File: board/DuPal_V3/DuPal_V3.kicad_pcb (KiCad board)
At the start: 2 copper layers, 124 parts, among them J1 ZIF Socket, J2 Debug Header, K1 G6K-2, Q1 2N3904, SW1 RESET, U1 Pico, U10 74HCT166, U11 74HCT166, U12 74HCT166, U13 SN74LV1T125DBV, U2 74HCT595, U3 74HCT595, U4 74HCT595, U5 74HCT595, U6 74HCT595, U7 74HCT02, U8 74HCT166, U9 74HCT166

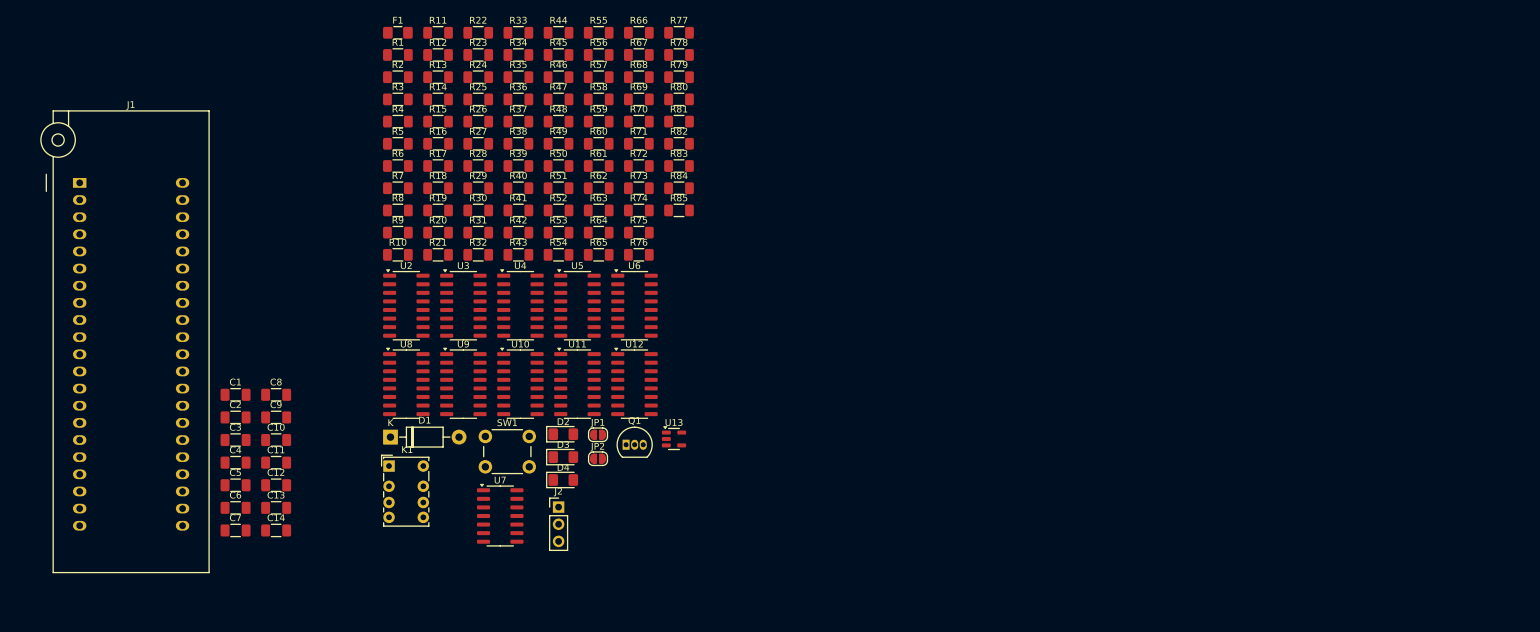
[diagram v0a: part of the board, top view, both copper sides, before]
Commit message: Begin organizing the footprint
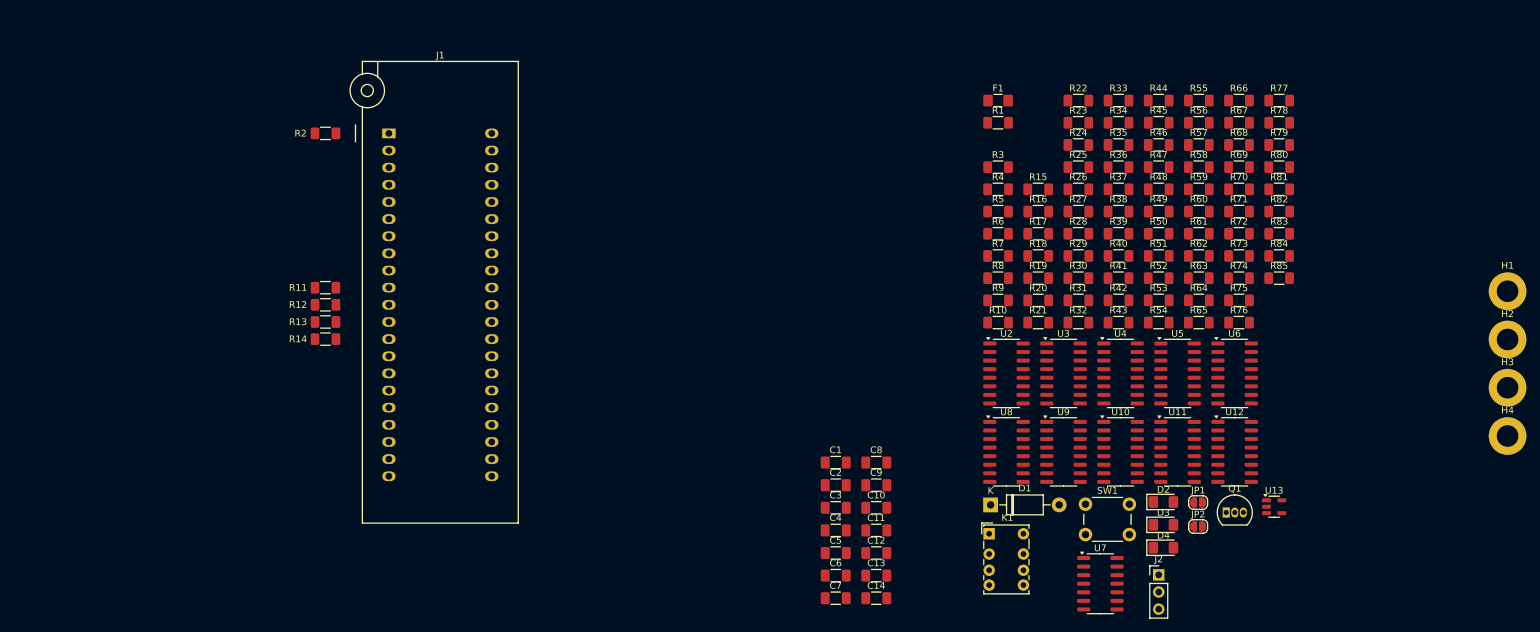
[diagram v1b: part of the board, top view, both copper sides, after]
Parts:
- added H1: MountingHole_Pad, MountingHole:MountingHole_3.2mm_M3_DIN965_Pad, F.Cu at (291.6, 79.8)
- added H2: MountingHole_Pad, MountingHole:MountingHole_3.2mm_M3_DIN965_Pad, F.Cu at (291.6, 86.9)
- added H3: MountingHole_Pad, MountingHole:MountingHole_3.2mm_M3_DIN965_Pad, F.Cu at (291.6, 94.1)
- added H4: MountingHole_Pad, MountingHole:MountingHole_3.2mm_M3_DIN965_Pad, F.Cu at (291.6, 101.2)
- R43: value 1K -> 1.2K
- moved F1 89.5 mm to (216.1, 51.5)
- moved R1 89.5 mm to (216.1, 54.8)
- moved R10 89.5 mm to (216.1, 84.4)
- moved R3 89.5 mm to (216.1, 61.4)
- moved R4 89.5 mm to (216.1, 64.7)
- moved R5 89.5 mm to (216.1, 68.0)
- moved R6 89.5 mm to (216.1, 71.3)
- moved R7 89.5 mm to (216.1, 74.5)
- moved R8 89.5 mm to (216.1, 77.8)
- moved R9 89.5 mm to (216.1, 81.1)
- moved C1 89.5 mm to (192.1, 105.2)
- moved C2 89.5 mm to (192.1, 108.5)
- moved C3 89.5 mm to (192.1, 111.9)
- moved C4 89.5 mm to (192.1, 115.2)
- moved C5 89.5 mm to (192.1, 118.6)
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
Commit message: Some more placing on the PCB
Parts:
- moved R15 108.5 mm to (116.5, 89.4)
- moved R16 108.3 mm to (116.5, 91.9)
- moved R17 108.1 mm to (116.5, 94.5)
- moved R18 108.0 mm to (116.5, 97.0)
- moved R19 107.8 mm to (116.5, 99.6)
- moved R20 107.7 mm to (116.5, 102.1)
- moved R21 107.5 mm to (116.5, 104.6)
- moved R10 99.9 mm to (116.5, 76.7)
- moved R9 99.9 mm to (116.5, 74.2)
- moved R8 99.8 mm to (116.5, 71.6)
- moved R7 99.8 mm to (116.5, 69.1)
- moved R6 99.8 mm to (116.5, 66.5)
- moved R5 99.7 mm to (116.5, 64.0)
- moved R4 99.7 mm to (116.5, 61.5)
- moved R3 99.7 mm to (116.5, 58.9)
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
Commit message: More board placing
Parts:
- R42, R46: moved to B.Cu
- moved R46 123.5 mm to (116.5, 56.4), turned to 180 degrees
- moved R33 88.1 mm to (150.3, 79.2), turned to 180 degrees
- moved R42 87.2 mm to (150.4, 56.4), turned to 180 degrees
- moved R34 86.4 mm to (150.3, 76.7), turned to 180 degrees
- moved R41 85.7 mm to (150.4, 58.9), turned to 180 degrees
- moved R35 85.1 mm to (150.4, 74.2), turned to 180 degrees
- moved R40 84.6 mm to (150.4, 61.5), turned to 180 degrees
- moved R36 84.2 mm to (150.4, 71.6), turned to 180 degrees
- moved R39 83.9 mm to (150.4, 64.0), turned to 180 degrees
- moved R37 83.7 mm to (150.4, 69.1), turned to 180 degrees
- moved R38 83.6 mm to (150.4, 66.5), turned to 180 degrees
- moved R27 82.0 mm to (150.4, 94.5), turned to 180 degrees
- moved R28 80.4 mm to (150.4, 91.9), turned to 180 degrees
- moved R29 79.1 mm to (150.4, 89.4), turned to 180 degrees
- moved R30 78.2 mm to (150.4, 86.9), turned to 180 degrees
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
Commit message: More placing
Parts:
- R47, R48, R49, R50, R51: moved to B.Cu
- moved R51 123.6 mm to (116.5, 69.1), turned to 180 degrees
- moved R50 123.5 mm to (116.5, 66.5), turned to 180 degrees
- moved R49 123.5 mm to (116.5, 64.0), turned to 180 degrees
- moved R48 123.5 mm to (116.5, 61.5), turned to 180 degrees
- moved R47 123.5 mm to (116.5, 58.9), turned to 180 degrees

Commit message: Update board
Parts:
- R46, R47, R48, R49, R50, R51, R53, R54, R55, R56, R57, R58, R59, R60, R61, R62, R63, R64, R65, R66, R67, R68, R69, R70, R71, R72, R73, R74, R75, R76, R77, R78, R79, R80, R81, R82, R83, R84, R85: value 100K -> 470K
- R52: value 100K -> 470K; moved to B.Cu
- moved R52 123.6 mm to (116.5, 71.6), turned to 180 degrees

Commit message: More placements
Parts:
- R53, R54, R55, R56, R57, R58, R59, R60, R61, R62, R63, R64, R65, R66, U10, U11, U12, U8, U9: moved to B.Cu
- moved R55 132.3 mm to (116.5, 79.2), turned to 180 degrees
- moved R56 132.2 mm to (116.5, 81.8), turned to 180 degrees
- moved R57 132.0 mm to (116.5, 84.3), turned to 180 degrees
- moved R58 131.9 mm to (116.5, 86.9), turned to 180 degrees
- moved R59 131.7 mm to (116.5, 89.4), turned to 180 degrees
- moved R60 131.6 mm to (116.5, 91.9), turned to 180 degrees
- moved R61 131.5 mm to (116.5, 94.5), turned to 180 degrees
- moved R62 131.3 mm to (116.5, 97.0), turned to 180 degrees
- moved R63 131.2 mm to (116.5, 99.6), turned to 180 degrees
- moved R64 131.1 mm to (116.5, 102.1), turned to 180 degrees
- moved R65 131.0 mm to (116.5, 104.6), turned to 180 degrees
- moved R54 123.7 mm to (116.5, 76.7), turned to 180 degrees
- moved R53 123.6 mm to (116.5, 74.2), turned to 180 degrees
- moved U12 123.2 mm to (133.9, 65.9)
- moved U11 109.2 mm to (133.9, 93.7)
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
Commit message: Initial placement on board
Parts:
- C1, C2, C3, C4, C5, C6, C7, JP1, JP2, R67, R68, R69, R70, R71, R72, R73, R74, R75, R76, R77, R78, R79, R80, R81, R82, R83, R84, R85: moved to B.Cu
- moved H3 200.4 mm to (97.3, 45.0)
- moved H4 194.5 mm to (97.3, 109.2)
- moved U1 147.8 mm to (190.1, 88.3), turned to 180 degrees
- moved D2 142.7 mm to (114.1, 45.0), turned to 90 degrees
- moved R43 124.7 mm to (114.1, 50.1), turned to -90 degrees
- moved U3 123.9 mm to (102.0, 96.8)
- moved U2 120.3 mm to (102.0, 57.9)
- moved JP1 117.5 mm to (146.1, 48.8)
- moved JP2 116.5 mm to (149.7, 48.8), turned to 180 degrees
- moved R67 115.2 mm to (146.8, 102.0)
- moved R77 113.8 mm to (146.7, 76.6)
- moved R85 113.1 mm to (146.8, 56.3)
- moved R68 112.9 mm to (146.8, 99.4)
- moved Q1 112.9 mm to (158.2, 46.7), turned to -90 degrees
- moved R78 112.7 mm to (146.7, 74.0)
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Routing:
- net /ZIF_9: vias 0 -> 1
- net /ZIF_8: vias 0 -> 1
- net /ZIF_7: vias 0 -> 1
- net /ZIF_6: vias 0 -> 1
- net /ZIF_5: vias 0 -> 1
- net /ZIF_41: vias 0 -> 1
- net /ZIF_40: vias 0 -> 1
- net /ZIF_4: vias 0 -> 1
- net /ZIF_39: vias 0 -> 1
- net /ZIF_38: vias 0 -> 1
- net /ZIF_37: vias 0 -> 1
- net /ZIF_36: vias 0 -> 1
- net /ZIF_35: vias 0 -> 1
- net /ZIF_34: vias 0 -> 1
- net /ZIF_33: vias 0 -> 1
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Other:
- board outline added: 116.8 x 73.7 mm

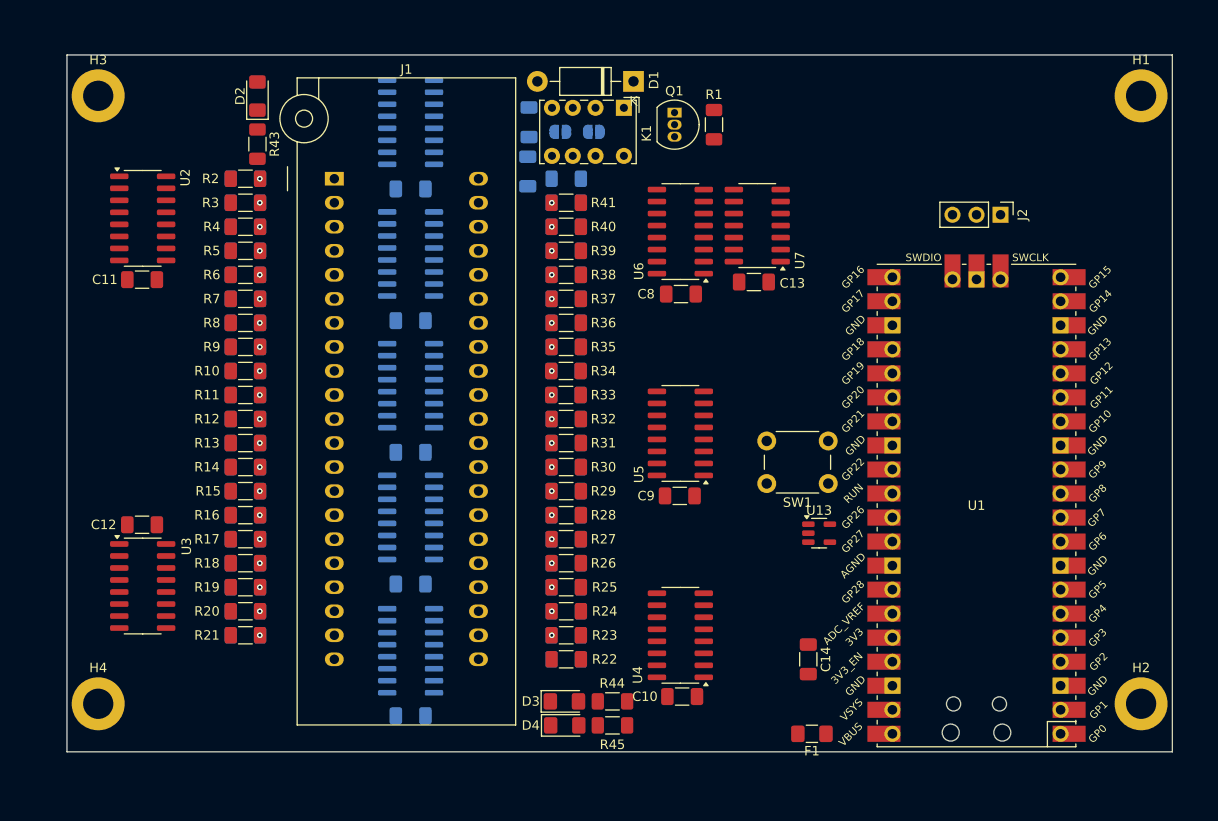
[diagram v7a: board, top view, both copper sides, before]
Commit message: First automatic routing of the board
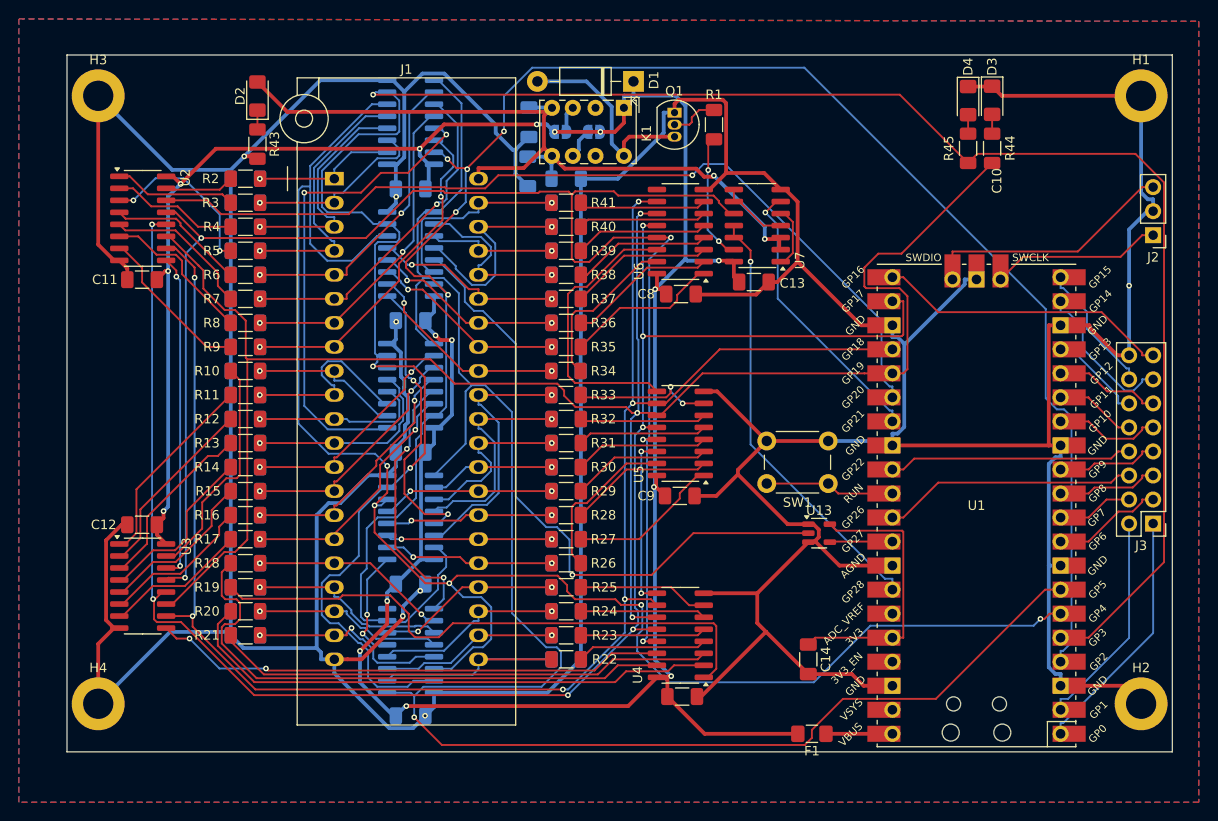
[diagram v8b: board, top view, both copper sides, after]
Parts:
- added J3: Extra, Connector_PinHeader_2.54mm:PinHeader_2x08_P2.54mm_Vertical, F.Cu at (208.8, 90.2)
- moved D4 78.6 mm to (189.2, 45.5), turned to -90 degrees
- moved D3 78.0 mm to (191.8, 45.4), turned to -90 degrees
- moved R45 71.7 mm to (189.2, 50.5), turned to 90 degrees
- moved R44 70.9 mm to (191.8, 50.5), turned to 90 degrees
- moved J2 16.3 mm to (208.8, 59.7), turned to 180 degrees
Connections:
- U1 pad 1: unconnected-(U1-GPIO0-Pad1) -> /GPIO0
- U1 pad 10: unconnected-(U1-GPIO7-Pad10)_0 -> /GPIO7
- U1 pad 11: unconnected-(U1-GPIO8-Pad11)_0 -> /GPIO8
- U1 pad 12: unconnected-(U1-GPIO9-Pad12)_0 -> /GPIO9
- U1 pad 14: unconnected-(U1-GPIO10-Pad14)_0 -> /GPIO10
- U1 pad 15: unconnected-(U1-GPIO11-Pad15)_0 -> /GPIO11
- U1 pad 16: unconnected-(U1-GPIO12-Pad16)_0 -> /GPIO12
- U1 pad 17: unconnected-(U1-GPIO13-Pad17) -> /GPIO13
- U1 pad 19: unconnected-(U1-GPIO14-Pad19) -> /GPIO14
- U1 pad 2: unconnected-(U1-GPIO1-Pad2)_0 -> /GPIO1
- U1 pad 20: unconnected-(U1-GPIO15-Pad20) -> /GPIO15
- U1 pad 21: unconnected-(U1-GPIO16-Pad21) -> /GPIO16
- U1 pad 29: unconnected-(U1-GPIO22-Pad29) -> /GPIO22
- U1 pad 31: unconnected-(U1-GPIO26_ADC0-Pad31) -> /GPIO26
- U1 pad 9: unconnected-(U1-GPIO6-Pad9) -> /GPIO6
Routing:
- net GND: track 0.00 -> 662.5 mm, vias 0 -> 7
- net VCC: track 0.00 -> 288.9 mm, vias 0 -> 16
- net /PISO_CLK: track 0.00 -> 243.5 mm, vias 0 -> 3
- net /SIPO_CLK: track 0.00 -> 202.8 mm, vias 0 -> 3
- net /PISO_SH: track 0.00 -> 197.7 mm, vias 0 -> 5
- net /~{PISO_CLR}: track 0.00 -> 193.6 mm, vias 0 -> 1
- net /SIPO_RCLK: track 0.00 -> 183.0 mm, vias 0 -> 7
- net /PISO_INH: track 0.00 -> 178.4 mm, vias 0 -> 5
- net /~{SIPO_CLR}: track 0.00 -> 177.2 mm, vias 0 -> 6
- net Net-(U2-~{OE}): track 0.00 -> 169.2 mm, vias 0 -> 5
- net /SIPO_SER: track 0.00 -> 94.1 mm, vias 0 -> 1
- net /SWITCHED_VCC: track 0.00 -> 84.4 mm, vias 0 -> 2
- net /PISO_SER: track 0.00 -> 67.6 mm, vias 0 -> 1
- net Net-(U4-QB): track 0.00 -> 61.8 mm
- net Net-(U4-QA): track 0.00 -> 59.9 mm
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- added copper zone on B.Cu, net GND
- added copper zone on F.Cu, net GND
